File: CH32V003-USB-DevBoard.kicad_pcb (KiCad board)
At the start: 2 copper layers, 15.8 x 26.1 mm, 25 parts, among them J1 USB_C_Receptacle_USB2.0, J2 Conn_01x10, J3 Conn_01x10, J4 Conn_01x01, SW1 SW_Push, U1 ME6211A33M3G-N, U3 CH32V003F4U6, Y1 24MHz

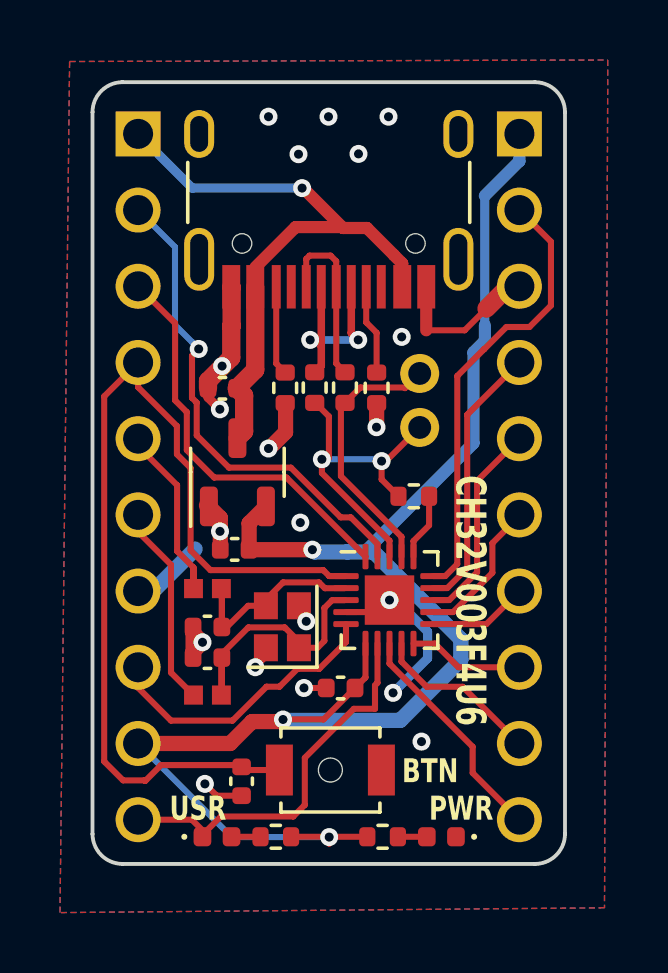
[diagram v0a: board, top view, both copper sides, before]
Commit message: Simplify design & switch to TSSOP-20 package for easier assembly
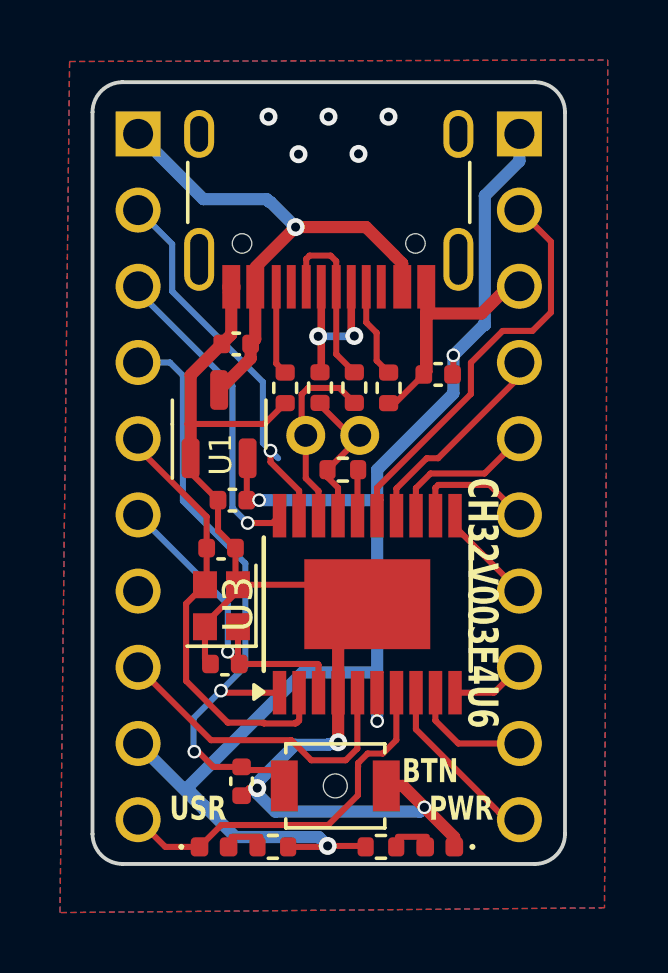
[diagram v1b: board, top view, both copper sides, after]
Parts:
- removed JP1, JP2: SolderJumper_2_Open, Library:SolderJumper_0402
- R8, R9: value 120R -> 120
- U3: footprint Package_DFN_QFN:QFN-20-1EP_3x3mm_P0.4mm_EP1.65x1.65mm -> Package_SO:ETSSOP-20-1EP_4.4x6.5mm_P0.65mm_EP3x4.2mm
- moved C3 10.9 mm to (152.7, 99.9)
- moved J4 2.99 mm to (149.3, 101.9), turned to 0 degrees
- moved C5 2.67 mm to (145.5, 105.7), turned to 180 degrees
- moved R1 2.53 mm to (149.5, 103.1)
- moved Y1 2.15 mm to (145.5, 107.6)
- moved U1 1.72 mm to (145.4, 101.6)
- moved C2 1.64 mm to (145.8, 104.1)
- moved C1 1.55 mm to (146.0, 98.9)
- moved U3 0.75 mm to (150.3, 107.6), turned to 90 degrees
- moved C4 0.62 mm to (145.6, 109.6)
- moved SW1 0.55 mm to (149.3, 113.6)
- moved R2 0.40 mm to (151.1, 100.4)
- moved R8 0.35 mm to (147.2, 115.7)
- moved D1 0.35 mm to (145.2, 115.7)
- moved D2 0.34 mm to (152.8, 115.7)
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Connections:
- net Net-(J1-D+-PadA6) renamed /D+
- net Net-(J1-D--PadA7) renamed /D-
- J2 pad 5: PA1_H -> PA1
- J2 pad 6: PA2_H -> PA2
- U3 pad 17: USB_DP -> USB_DN
- U3 pad 18: USB_DN -> USB_DP
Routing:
- net GND: track 26.3 -> 51.6 mm, vias 20 -> 8
- net PD7: track 32.5 -> 20.7 mm, vias 0 -> 2
- net PA1: track 6.97 -> 14.7 mm
- net PA1_H: track 6.31 -> 0.00 mm
- net PA2_H: track 6.21 -> 0.00 mm
- net +3V3: track 54.1 -> 48.2 mm, vias 3 -> 4
- net USB_DN: track 11.3 -> 5.44 mm, vias 2 -> 0
- net USB_DP: track 10.0 -> 6.46 mm
- net PD5: track 16.2 -> 12.8 mm
- net VBUS: track 20.4 -> 17.2 mm
- net PD6: track 13.6 -> 10.6 mm, vias 0 -> 1
- net PA2: track 8.32 -> 11.2 mm, vias 0 -> 1
- net PC6: track 6.89 -> 5.05 mm
- net PC7: track 8.99 -> 7.19 mm
- net PC1: track 7.66 -> 5.92 mm
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
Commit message: Minor updates & cleanup
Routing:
- net +3V3: track 48.2 -> 47.5 mm
- net GND: vias 8 -> 9
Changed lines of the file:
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@@
 	)
 	(gr_text "CH32V003\nUSB DevBoard\n"
-		(at 148.35 106 90)
+		(at 149.784 106.642 90)
 		(layer "B.SilkS")
 		(effects
@@
 	)
 	(gr_text "Rev. 1"
-		(at 149.9 106 90)
+		(at 151.334 106.642 90)
 		(layer "B.SilkS")
 		(effects
@@
 	)
 	(segment
+		(start 150.27325 107.63925)
+		(end 150.3425 107.57)
+		(width 0.2032)
+		(layer "F.Cu")
+		(net "GND")
+	)
+	(segment
 		(start 149.3725 108.54)
-		(end 150.3425 107.57)
+		(end 150.27325 107.63925)
 		(width 0.2032)
 		(layer "F.Cu")
@@
 		(width 0.2032)
 		(layer "F.Cu")
+		(net "GND")
+	)
+	(via
+		(at 150.27325 107.63925)
+		(size 0.4572)
+		(drill 0.3048)
+		(layers "F.Cu" "B.Cu")
 		(net "GND")
 	)
@@
 	)
 	(segment
+		(start 146.649293 111.381293)
+		(end 144.324093 113.706493)
+		(width 0.4064)
+		(layer "B.Cu")
+		(net "+3V3")
+	)
+	(segment
 		(start 144.9188 114.3012)
 		(end 144.9188 114.4282)
@@
 	)
 	(segment
+		(start 146.736 111.468)
+		(end 146.649293 111.381293)
+		(width 0.2032)
+		(layer "B.Cu")
+		(net "+3V3")
+	)
+	(segment
 		(start 153.213 100.546)
 		(end 150.673 103.086)
@@
 	)
 	(segment
-		(start 148.188185 109.8424)
-		(end 144.324093 113.706493)
-		(width 0.4064)
-		(layer "B.Cu")
-		(net "+3V3")
-	)
-	(segment
 		(start 155.4132 91.8926)
 		(end 155.4132 92.801728)
@@
 	)
 	(segment
-		(start 150.673 111.468)
-		(end 150.673 104.102)
-		(width 0.4064)
-		(layer "B.Cu")
-		(net "+3V3")
-	)
-	(segment
 		(start 144.324093 113.706493)
 		(end 144.9188 114.3012)
@@
 	)
 	(segment
-		(start 150.673 109.8424)
-		(end 148.188185 109.8424)
+		(start 150.673 111.468)
+		(end 146.736 111.468)
+		(width 0.4064)
+		(layer "B.Cu")
+		(net "+3V3")
+	)
+	(segment
+		(start 146.736 111.294586)
+		(end 146.649293 111.381293)
+		(width 0.4064)
+		(layer "B.Cu")
+		(net "+3V3")
+	)
+	(segment
+		(start 146.736 104.102)
+		(end 146.736 111.294586)
 		(width 0.4064)
 		(layer "B.Cu")
@@
 	)
 	(segment
-		(start 146.355 104.864)
+		(start 145.974 104.864)
 		(end 147.1785 104.864)
 		(width 0.2032)
@@
 	)
 	(via
-		(at 146.355 104.864)
+		(at 145.974 104.864)
 		(size 0.4572)
 		(drill 0.3048)
@@
 	)
 	(segment
+		(start 145.847 104.737)
+		(end 145.847 100.292)
+		(width 0.2032)
+		(layer "B.Cu")
+		(net "PD6")
+	)
+	(segment
+		(start 145.847 100.292)
+		(end 142.7032 97.1482)
+		(width 0.2032)
+		(layer "B.Cu")
+		(net "PD6")
+	)
+	(segment
 		(start 142.7032 97.1482)
-		(end 145.847 100.292)
+		(end 142.7032 96.9726)
 		(width 0.2032)
 		(layer "B.Cu")
@@
 	)
 	(segment
-		(start 142.7032 96.9726)
-		(end 142.7032 97.1482)
-		(width 0.2032)
-		(layer "B.Cu")
-		(net "PD6")
-	)
-	(segment
-		(start 145.847 104.356)
-		(end 146.355 104.864)
-		(width 0.2032)
-		(layer "B.Cu")
-		(net "PD6")
-	)
-	(segment
-		(start 145.847 100.292)
-		(end 145.847 104.356)
+		(start 145.974 104.864)
+		(end 145.847 104.737)
 		(width 0.2032)
 		(layer "B.Cu")
@@
 		(net "GND")
 		(layers "F.Cu" "B.Cu")
+		(name "GND")
 		(hatch edge 0.5)
 		(connect_pads
